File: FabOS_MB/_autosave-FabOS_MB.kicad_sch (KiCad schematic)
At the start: 2 parts

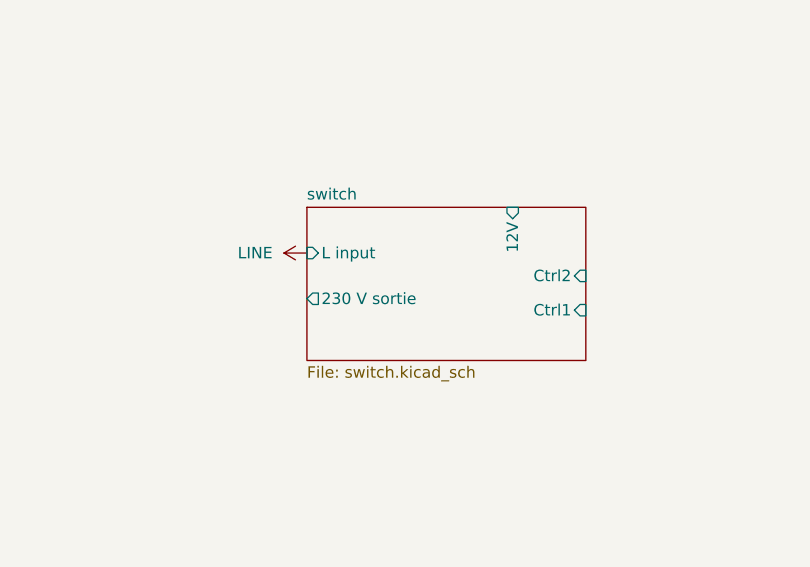
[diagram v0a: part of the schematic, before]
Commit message: Déplacement du switch dans un projet PCB_Power
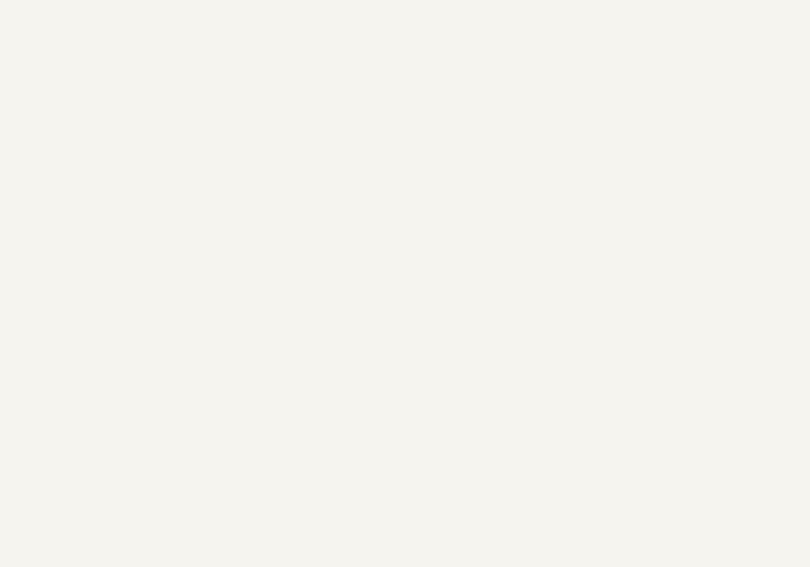
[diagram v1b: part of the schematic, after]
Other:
- removed sheet switch
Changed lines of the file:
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@@
-	)
-	(symbol
-		(lib_id "power:LINE")
-		(at 228.6 144.78 90)
-		(unit 1)
-		(exclude_from_sim no)
-		(in_bom yes)
-		(on_board yes)
-		(dnp no)
-		(fields_autoplaced yes)
-		(property "Reference" "#PWR055"
-			(at 232.41 144.78 0)
-			(effects
-				(font
-					(size 1.27 1.27)
-				)
-				(hide yes)
-			)
-		)
-		(property "Value" "LINE"
-			(at 224.79 144.7799 90)
-			(effects
-				(font
-					(size 1.27 1.27)
-				)
-				(justify left)
-			)
-		)
-		(property "Footprint" ""
-			(at 228.6 144.78 0)
-			(effects
-				(font
-					(size 1.27 1.27)
-				)
-				(hide yes)
-			)
-		)
-		(property "Datasheet" ""
-			(at 228.6 144.78 0)
-			(effects
-				(font
-					(size 1.27 1.27)
-				)
-				(hide yes)
-			)
-		)
-		(property "Description" "Power symbol creates a global label with name \"LINE\""
-			(at 228.6 144.78 0)
-			(effects
-				(font
-					(size 1.27 1.27)
-				)
-				(hide yes)
-			)
-		)
-		(pin "1"
-		)
-		(instances
-			(project ""
-				(path "/09377d5d-727f-4ff4-92c8-7a0483d23f1e"
-					(reference "#PWR055")
-					(unit 1)
-				)
-			)
-		)
 	)
 	(symbol
@@
 				)
 			)
-		)
-	)
-	(sheet
-		(at 228.6 139.7)
-		(size 30.988 17.018)
-		(fields_autoplaced yes)
-		(stroke
-			(width 0.1524)
-			(type solid)
-		)
-		(fill
-			(color 0 0 0 0.0000)
-		)
-		(property "Sheetname" "switch"
-			(at 228.6 138.9884 0)
-			(effects
-				(font
-					(size 1.27 1.27)
-				)
-				(justify left bottom)
-			)
-		)
-		(property "Sheetfile" "switch.kicad_sch"
-			(at 228.6 157.3026 0)
-			(effects
-				(font
-					(size 1.27 1.27)
-				)
-				(justify left top)
-			)
-		)
-		(pin "12V" input
-			(at 251.46 139.7 90)
-			(effects
-				(font
-					(size 1.27 1.27)
-				)
-				(justify right)
-			)
-		)
-		(pin "L input" input
-			(at 228.6 144.78 180)
-			(effects
-				(font
-					(size 1.27 1.27)
-				)
-				(justify left)
-			)
-		)
-		(pin "230 V sortie" output
-			(at 228.6 149.86 180)
-			(effects
-				(font
-					(size 1.27 1.27)
-				)
-				(justify left)
-			)
-		)
-		(pin "Ctrl1" input
-			(at 259.588 151.13 0)
-			(effects
-				(font
-					(size 1.27 1.27)
-				)
-				(justify right)
-			)
-		)
-		(pin "Ctrl2" input
-			(at 259.588 147.32 0)
-			(effects
-				(font
-					(size 1.27 1.27)
-				)
-				(justify right)
-			)
-		)
-		(instances
-			(project "FabOS_MB"
-				(path "/09377d5d-727f-4ff4-92c8-7a0483d23f1e"
-					(page "4")
-				)
-			)
